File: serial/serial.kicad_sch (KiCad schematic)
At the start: 34 parts, among them J1 Conn_02x20_Odd_Even, J2 D-SUB Male 9 pins, U1 74LS30, U2 74LS02, U3 74LS00, U4 MC6850, U5 CD4060BE, U6 MAX232, Y1 4.0Mhz

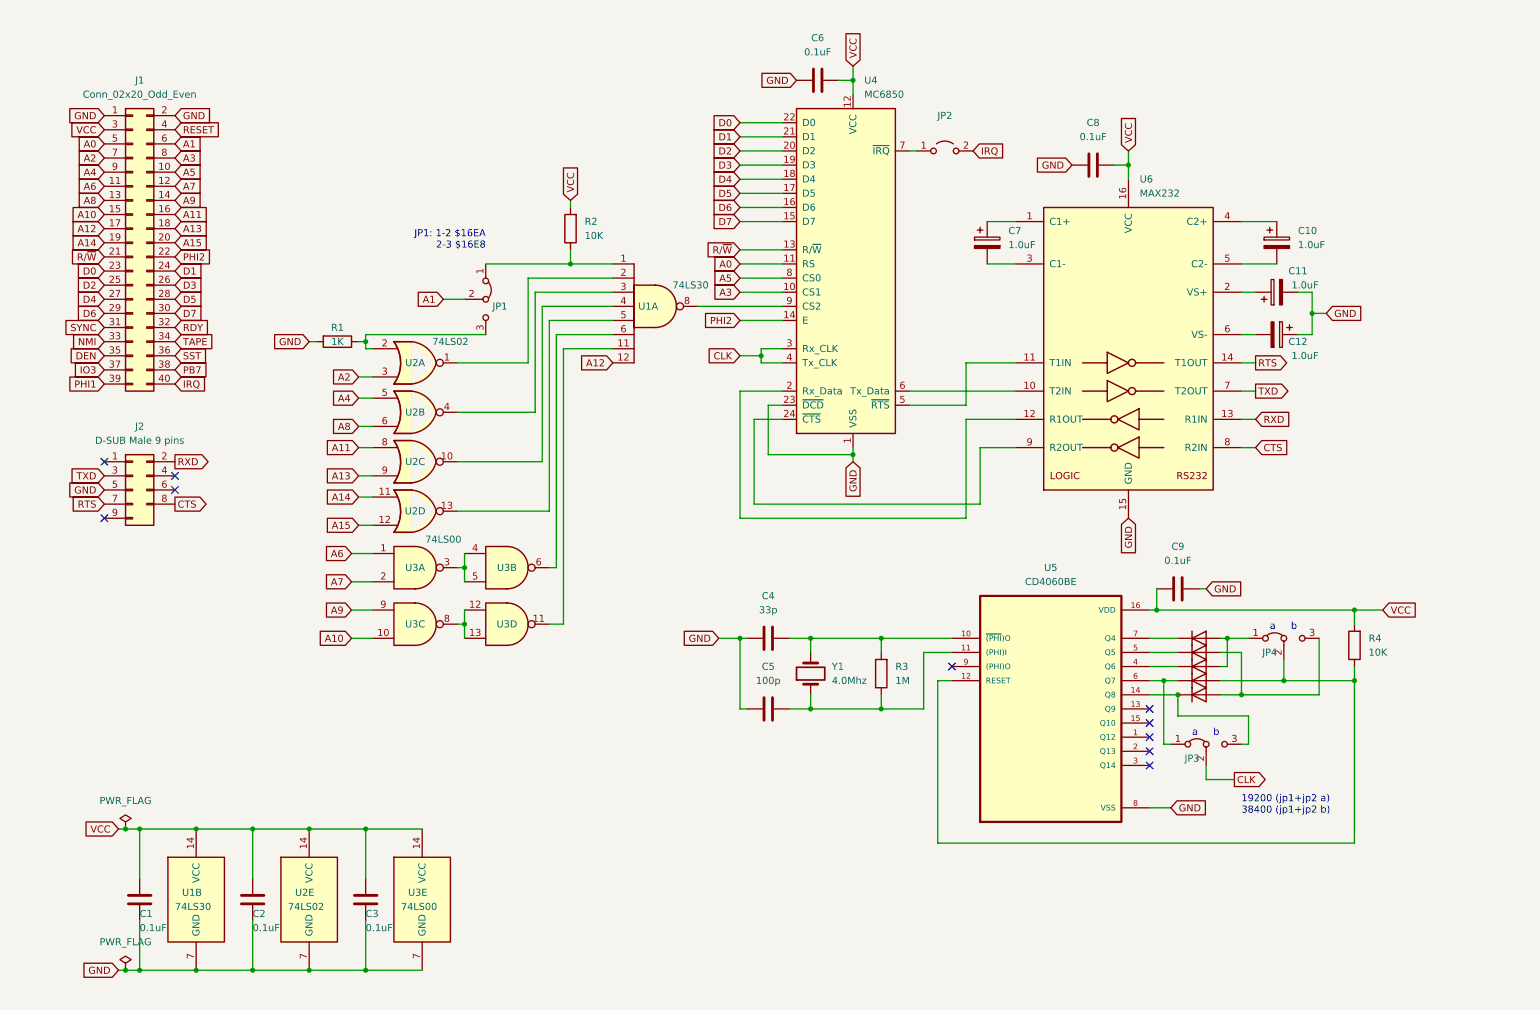
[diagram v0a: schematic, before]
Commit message: Add TTL header
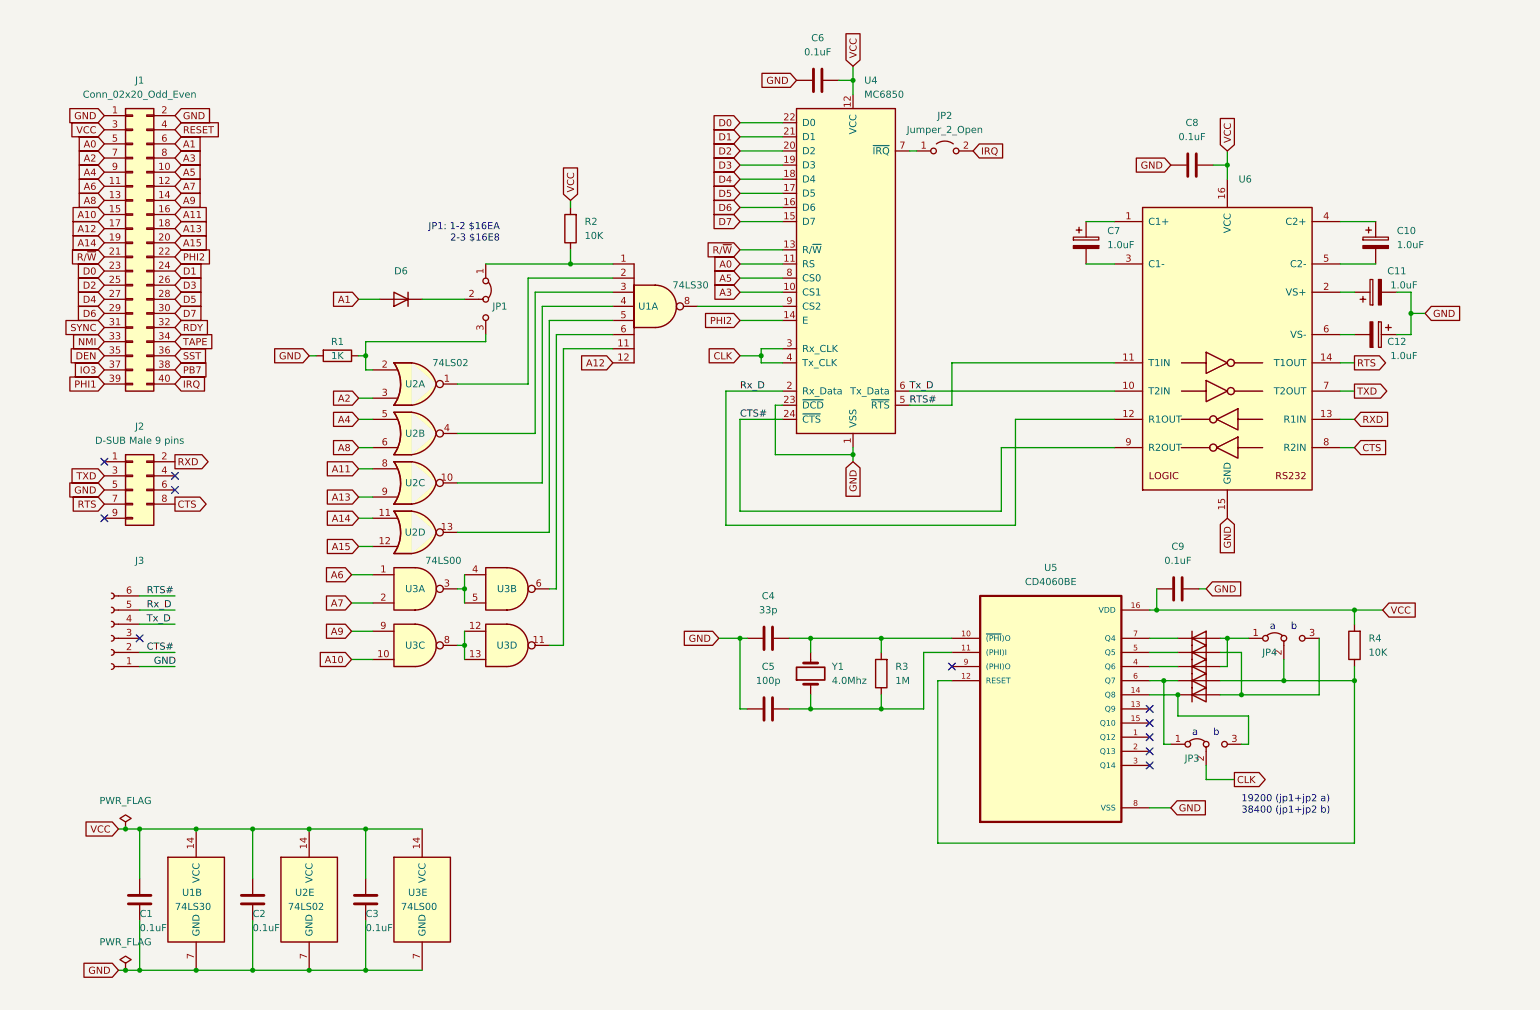
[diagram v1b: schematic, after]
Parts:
- added D6: (no value), symbol Diode:1N4148
- added J3: (no value), symbol Connector:Conn_01x06_Female
- JP1: value (none) -> addr select; footprint (none) -> Connector_PinHeader_2.54mm:PinHeader_1x03_P2.54mm_Vertical
- JP2: value (none) -> Jumper_2_Open; footprint (none) -> Connector_PinHeader_2.54mm:PinHeader_1x02_P2.54mm_Vertical
- JP3, JP4: value (none) -> Jumper_3_Bridged12; footprint (none) -> Connector_PinHeader_2.54mm:PinHeader_1x03_P2.54mm_Vertical
- U6: value MAX232 -> (none); footprint Package_DIP:DIP-16_W7.62mm -> (none)
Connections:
- net A1: now also D6.2 (A); no longer JP1.2 (C)
- net GND: now also J3.1 (Pin_1)
- net Rx_D: now reaches U4.2 (Rx_Data), U6.12 (R1OUT)
- net Rx_D: now also J3.5 (Pin_5)
- net CTS#: now reaches U4.24 (~{CTS}), U6.9 (R2OUT)
- net CTS#: now also J3.2 (Pin_2)
- net RTS#: now reaches U4.5 (~{RTS}), U6.11 (T1IN)
- net RTS#: now also J3.6 (Pin_6)
- net Tx_D: now reaches U4.6 (Tx_Data), U6.10 (T2IN)
- net Tx_D: now also J3.4 (Pin_4)
- new net: D6.1 (K), JP1.2 (C)
- no-connect marks 10 -> 11
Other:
- moved on the sheet: C10, C11, C12, C7, C8, R1, U2A, U2B, U2C, U2D, U3A, U3B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

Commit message: Minor improvements
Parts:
- removed D6: (no value), symbol Diode:1N4148
- removed J3: (no value), symbol Connector:Conn_01x06_Female
- removed R1: 1K, Resistor_THT:R_Axial_DIN0207_L6.3mm_D2.5mm_P7.62mm_Horizontal, symbol Device:R
- removed R2: 10K, Resistor_THT:R_Axial_DIN0207_L6.3mm_D2.5mm_P7.62mm_Horizontal, symbol Device:R
- removed U3: 74LS00, Package_DIP:DIP-14_W7.62mm, symbol 74xx:74LS00
- added J3: Conn_01x06_Male, Connector_PinHeader_2.54mm:PinHeader_1x06_P2.54mm_Horizontal, symbol Connector:Conn_01x06_Male
- added U3: 74LS02, Package_DIP:DIP-14_W7.62mm, symbol 74xx:74LS02
- C7: renamed from C4; value 33p -> 33pF
- C8: renamed from C5; value 100p -> 100pF
- U6: value (none) -> MAX232; footprint (none) -> Package_DIP:DIP-16_W7.62mm
- renumbered C6 to C4, C9 to C5, C8 to C6, C7 to C9, R3 to R1, R4 to R2
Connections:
- net A1: now also JP1.3 (B), U3.8, U3.9
- net A10: now also U3.6
- net A6: now also U3.2
- net A7: now also U3.3
- net A9: now also U3.5
- net CTS#: now also J3.6 (Pin_6)
- net GND: now also U2.2, J3.1 (Pin_1), U3.11, U3.12, U3.7 (GND)
- net RTS#: now also J3.2 (Pin_2)
- net Rx_D: now also J3.4 (Pin_4)
- net Tx_D: now also J3.5 (Pin_5)
- net VCC: now also U3.14 (VCC)
- net at JP1.2 (C): now also U1.1
- net at JP1.1 (A): now also U3.10; no longer U1.1
- net at U1.11: now also U3.4
- net at U1.6: now also U3.1
- no-connect marks 11 -> 12
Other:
- note added: "JP1: 1-2 $16E8 2-3 $16EA"
- note removed: "JP1: 1-2 $16EA 2-3 $16E8"
- moved on the sheet: C7, C8, C9, JP1, R1, U2A, U2B, U2C, U2D, Y1

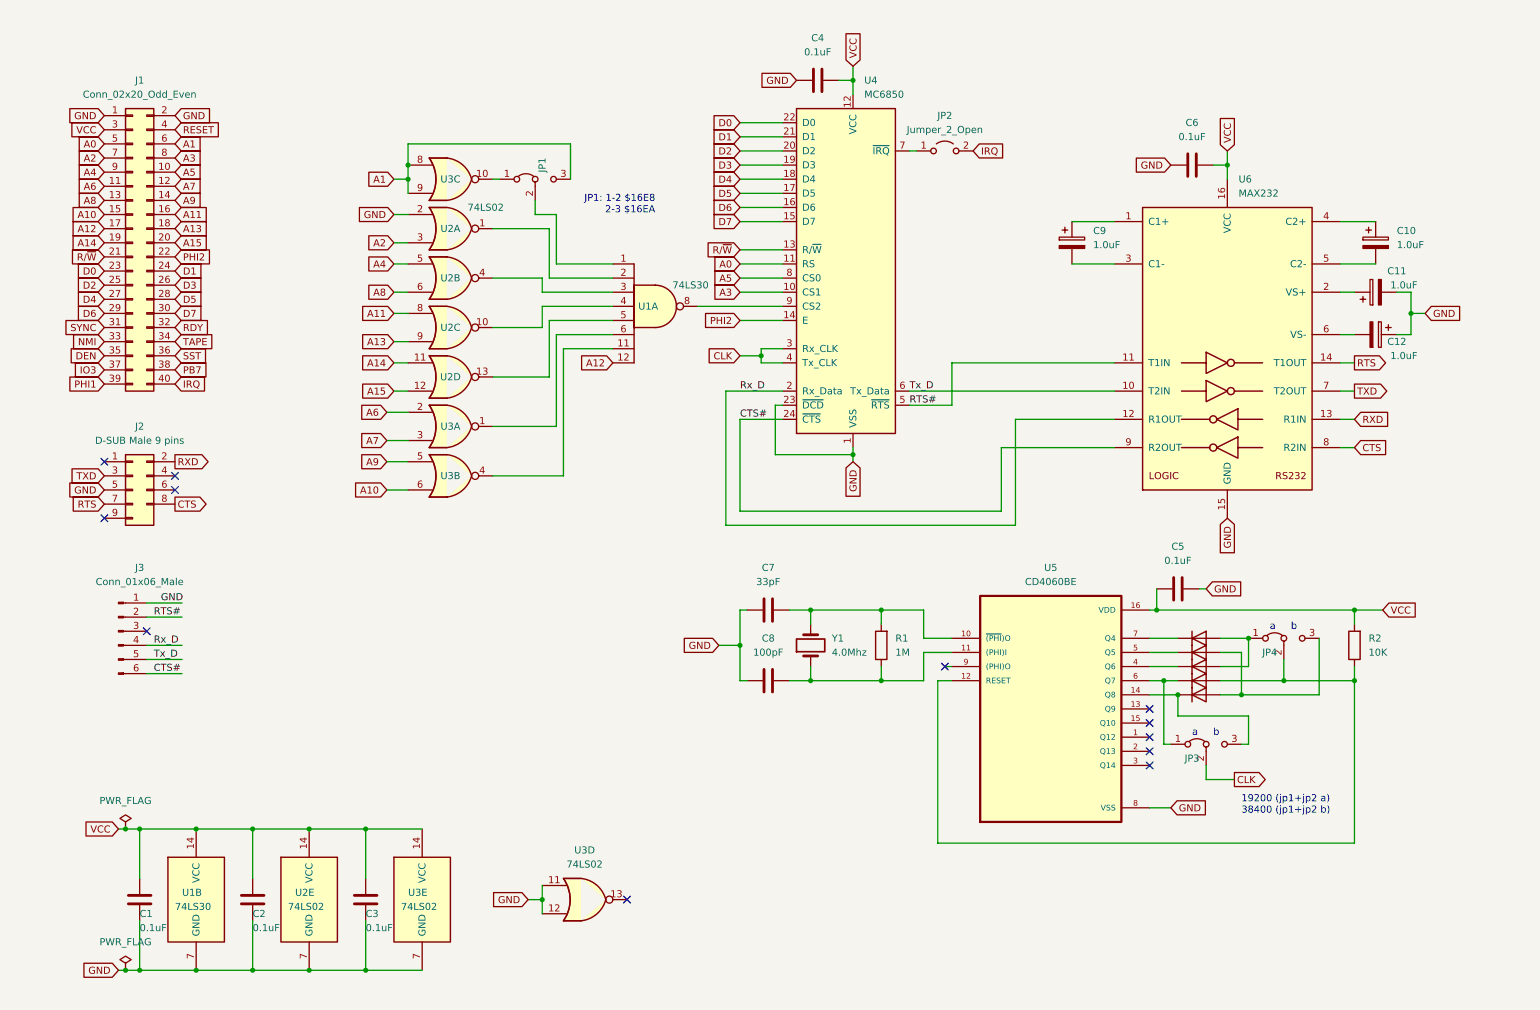
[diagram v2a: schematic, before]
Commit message: Update schematic to enable 9.6-38.4kHz clock
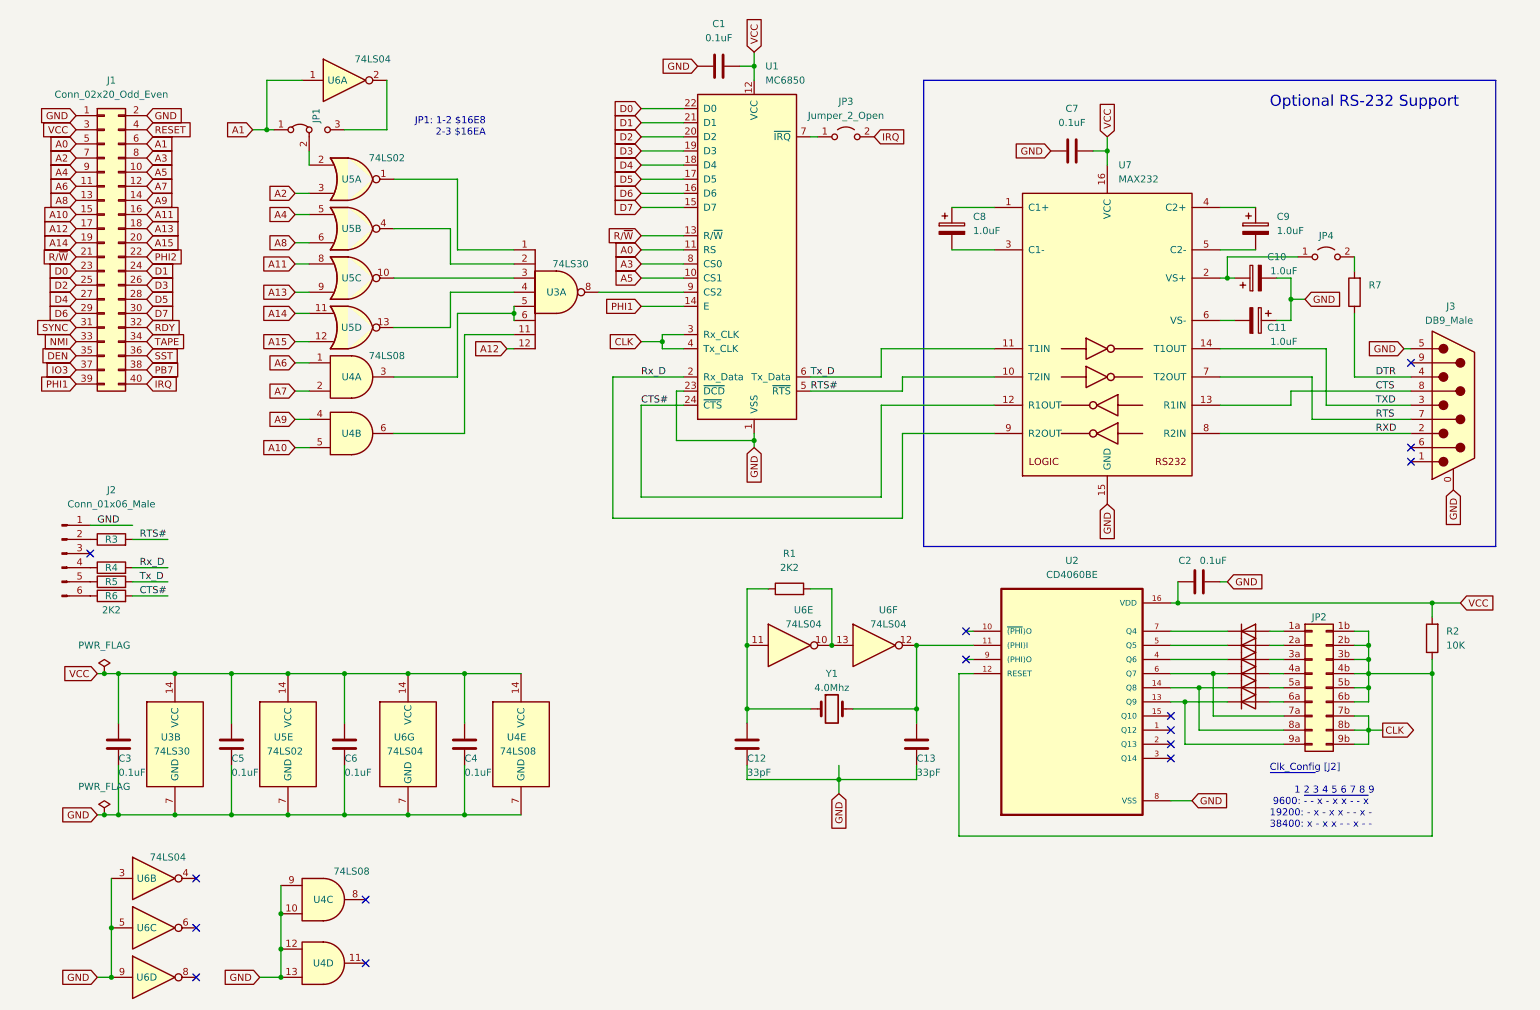
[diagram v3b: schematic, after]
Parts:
- removed C7: 33pF, Capacitor_THT:C_Disc_D4.3mm_W1.9mm_P5.00mm, symbol Device:C
- removed C8: 100pF, Capacitor_THT:C_Disc_D4.3mm_W1.9mm_P5.00mm, symbol Device:C
- removed J2: D-SUB Male 9 pins, Connector_Dsub:DSUB-9_Male_Horizontal_P2.77x2.84mm_EdgePinOffset7.70mm_Housed_MountingHolesOffset9.12mm, symbol Connector_Generic:Conn_2Rows-09Pins
- removed JP3, JP4: Jumper_3_Bridged12, Connector_PinHeader_2.54mm:PinHeader_1x03_P2.54mm_Vertical, symbol Jumper:Jumper_3_Bridged12
- removed U3: 74LS02, Package_DIP:DIP-14_W7.62mm, symbol 74xx:74LS02
- added C12, C13: 33pF, Capacitor_THT:C_Disc_D3.0mm_W1.6mm_P2.50mm, symbol Device:C
- added C4: 0.1uF, Capacitor_THT:C_Disc_D3.0mm_W1.6mm_P2.50mm, symbol Device:C
- added D6: 1N4148, Diode_THT:D_DO-35_SOD27_P7.62mm_Horizontal, symbol Diode:1N4148
- added J3: DB9_Male, Connector_Dsub:DSUB-9_Male_Horizontal_P2.77x2.84mm_EdgePinOffset7.70mm_Housed_MountingHolesOffset9.12mm, symbol Connector:DB9_Male_MountingHoles
- added JP2: (no value), symbol Connector_Generic:Conn_02x09_Row_Letter_Last
- added JP4: Jumper_2_Open, Connector_PinHeader_2.54mm:PinHeader_1x02_P2.54mm_Vertical, symbol Jumper:Jumper_2_Open
- added R3, R4, R5, R6: 2K2, Resistor_THT:R_Axial_DIN0207_L6.3mm_D2.5mm_P7.62mm_Horizontal, symbol Device:R
- added R7: ~, Resistor_THT:R_Axial_DIN0207_L6.3mm_D2.5mm_P7.62mm_Horizontal, symbol Device:R
- added U4: 74LS08, symbol 74xx:74LS08
- added U6: 74LS04, Package_DIP:DIP-14_W7.62mm, symbol 74xx:74LS04
- R1: value 1M -> 2K2
- Y1: footprint Crystal:Crystal_HC49-4H_Vertical -> Crystal:Crystal_HC49-U_Vertical
- renumbered C4 to C1, C11 to C10, C12 to C11, C5 to C2, C1 to C3, C2 to C5, C3 to C6, C6 to C7, C9 to C8, C10 to C9, J3 to J2, JP2 to JP3, U4 to U1, U5 to U2, U1 to U3, U2 to U5, U6 to U7
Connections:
- net A1: now also JP1.1 (A), U6.1; no longer JP1.3 (B)
- net A10: now also U4.5
- net A3: now also U1.8 (CS0); no longer U1.10 (CS1)
- net A5: now also U1.10 (CS1); no longer U1.8 (CS0)
- net A6: now also U4.1
- net A7: now also U4.2
- net A9: now also U4.4
- net CLK: now also JP2.7b (Pin_7b), JP2.8b (Pin_8b), JP2.9b (Pin_9b)
- net CTS: now also U7.13 (R1IN), J3.8; no longer U7.8 (R2IN)
- net CTS#: now also U7.12 (R1OUT), R6.2; no longer J2.6 (Pin_6), U7.9 (R2OUT)
- net GND: now also C12.1, C13.1, C4.1, J3.0 (PAD), J3.5, U4.10, U4.12, U4.13, U4.7 (GND), U4.9, U6.3, U6.5, U6.7 (GND), U6.9; no longer U5.2
- net PHI1: now also U1.14 (E)
- net PHI2: no longer U1.14 (E)
- net RTS: now also U7.7 (T2OUT), J3.7; no longer U7.14 (T1OUT)
- net RTS#: now also U7.10 (T2IN), R3.2; no longer J2.2 (Pin_2), U7.11 (T1IN)
- net RXD: now also U7.8 (R2IN), J3.2; no longer U7.13 (R1IN)
- net Rx_D: now also U7.9 (R2OUT), R4.2; no longer J2.4 (Pin_4), U7.12 (R1OUT)
- net TXD: now also U7.14 (T1OUT), J3.3; no longer U7.7 (T2OUT)
- net Tx_D: now also U7.11 (T1IN), R5.2; no longer J2.5 (Pin_5), U7.10 (T2IN)
- net VCC: now also C4.2, U4.14 (VCC), U6.14 (VCC)
- net at D4.1 (K), U2.6 (Q7): now also JP2.7a (Pin_7a)
- net at R2.1, U2.12 (RESET): now also JP2.1b (Pin_1b), JP2.2b (Pin_2b), JP2.3b (Pin_3b), JP2.4b (Pin_4b), JP2.5b (Pin_5b), JP2.6b (Pin_6b); no longer D4.2 (A)
- net at D1.2 (A): now also JP2.1a (Pin_1a); no longer D3.2 (A)
- net at D2.2 (A): now also JP2.2a (Pin_2a); no longer D5.2 (A)
- net at U5.13: now also U3.4; no longer U3.5
- net at R1.1, Y1.1: now also C12.2, U6.11; no longer U2.11 ((PHI)I)
- net at U3.1: now also U5.1; no longer JP1.2 (C)
- net at U3.11: now also U4.6
- net at U3.2: now also U5.4; no longer U5.1
- net at U3.3: now also U5.10; no longer U5.4
- net at U3.6: now also U3.5, U4.3
- net at C10.1, U7.2 (VS+): now also JP4.1 (A)
- net at U2.13 (Q9): now also D6.1 (K), JP2.9a (Pin_9a)
- net at D5.1 (K), U2.14 (Q8): now also JP2.8a (Pin_8a)
- new net: D4.2 (A), JP2.4a (Pin_4a)
- new net: R1.2, U6.10, U6.13
- new net: JP4.2 (B), R7.2
- new net: JP1.2 (C), U5.2
- new net: JP1.3 (B), U6.2
- new net: C13.2, U2.11 ((PHI)I), U6.12, Y1.2
- new net: D3.2 (A), JP2.3a (Pin_3a)
- new net: D5.2 (A), JP2.5a (Pin_5a)
- new net: D6.2 (A), JP2.6a (Pin_6a)
- new net: J2.6 (Pin_6), R6.1
- new net: J2.2 (Pin_2), R3.1
- new net: J2.4 (Pin_4), R4.1
- new net: J2.5 (Pin_5), R5.1
- new net DTR: J3.4, R7.1
- now unconnected: U2.10 (~{(PHI})O)
- no-connect marks 12 -> 15
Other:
- note added: "Clk_Config [J2] ~{ } 1 2 3 4 5 6 7 8 9 9600: ~{- - x - x x - - x} 19200: - x - x x - - x - 38400: x - x x - - x - -"
- note added: "Optional RS-232 Support"
- note removed: "19200 (jp1+jp2 a) 38400 (jp1+jp2 b)"
- note removed: "a"
- note removed: "b"
- moved on the sheet: C1, C10, C11, C2, C3, C5, C6, C7, C8, C9, J1, J2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

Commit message: Route pcb
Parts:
- removed JP2: (no value), symbol Connector_Generic:Conn_02x09_Row_Letter_Last
- added JP2: Conn_02x09_Odd_Even, Connector_PinHeader_2.54mm:PinHeader_2x09_P2.54mm_Vertical, symbol Connector_Generic:Conn_02x09_Odd_Even
- renumbered R7 to R3, R3 to R4, R4 to R5, R5 to R6, R6 to R7
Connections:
- net CLK: now also JP2.14 (Pin_14), JP2.16 (Pin_16), JP2.18 (Pin_18)
- net at D4.1 (K), U2.6 (Q7): now also JP2.13 (Pin_13)
- net at D4.2 (A): now also JP2.7 (Pin_7)
- net at D1.2 (A): now also JP2.1 (Pin_1)
- net at R2.1, U2.12 (RESET): now also JP2.10 (Pin_10), JP2.12 (Pin_12), JP2.2 (Pin_2), JP2.4 (Pin_4), JP2.6 (Pin_6), JP2.8 (Pin_8)
- net at D6.1 (K), U2.13 (Q9): now also JP2.17 (Pin_17)
- net at D5.1 (K), U2.14 (Q8): now also JP2.15 (Pin_15)
- net at D2.2 (A): now also JP2.3 (Pin_3)
- net at D3.2 (A): now also JP2.5 (Pin_5)
- net at D5.2 (A): now also JP2.9 (Pin_9)
- net at D6.2 (A): now also JP2.11 (Pin_11)

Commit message: Update design
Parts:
- U6: value 74LS04 -> (none)
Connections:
- net A1: now also U6.9; no longer U6.1
- net GND: now also U2.12 (RESET), U6.1; no longer U6.9
- net PHI1: no longer U1.14 (E)
- net PHI2: now also U1.14 (E)
- net at JP2.10 (Pin_10), JP2.12 (Pin_12), JP2.2 (Pin_2)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: no longer U2.12 (RESET)
- net at JP1.3 (B): now also U6.8; no longer U6.2
